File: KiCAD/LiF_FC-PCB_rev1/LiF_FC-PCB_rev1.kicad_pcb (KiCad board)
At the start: 4 copper layers, 70 x 90 mm, 203 parts, among them J13 ESP_DGB_CONN, J14 CAN Upstream, J15 ESP_DGB_CONN, J16 ESP_DGB_CONN, J19 Load Cell, J22 CAN Upstream, J28 CAN Downstream, J31 CAN, J37 SKP OUT, J40 Door Closed, J43 Servo A, J44 Servo B, J45 Conn_01x10_Socket, J46 Conn_01x16_Pin, J47 Conn_01x16_Pin, J7 V_{IN}, Q1 MMBT4401, Q2 MMBT4401, SW1 Flash, SW2 Reset, SW3 CAN Termination, U1 AZ1117-3.3, U10 MCP2542FD-E/SN, U11 BMA400, U12 PAM8302AAS, U13 NCA9555, U14 SN74HC14DR, U15 SN74HC14DR, U16 NCA9555, U2 AZ1117-3.3, U3 TPS2117DRLR, U4 TPS2117DRLR, U5 LMR14050, U6 ESP32-S3-WROOM-1, U7 CY7C65213-28PVXI, U8 MCP6N11-xxxE/SN, U9 NCV8114ASN165T1G

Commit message: routing in progress. backup save
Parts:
- SW3, TP22, TP23, TP24, TP28: moved to B.Cu
- moved R1 117.9 mm to (157.2, 58.5), turned to 180 degrees
- moved R5 112.6 mm to (152.2, 58.5), turned to 180 degrees
- moved SW3 84.6 mm to (130.5, 62.0), turned to 0 degrees
- moved C33 82.9 mm to (136.5, 65.5)
- moved U10 82.7 mm to (132.5, 67.0)
- moved C34 82.4 mm to (134.0, 72.5)
- moved D15 81.9 mm to (135.8, 56.0)
- moved R53 81.5 mm to (132.5, 61.2)
- moved TP24 72.3 mm to (139.8, 66.0)
- moved TP22 64.1 mm to (136.2, 61.0)
- moved TP23 60.7 mm to (126.2, 61.0)
- moved R46 47.8 mm to (57.8, 122.2)
- moved R48 47.8 mm to (57.8, 116.3)
- moved R47 16.4 mm to (121.2, 55.5)
- moved R63 12.3 mm to (152.5, 74.8)
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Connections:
- J47 pad 12: /Stackup Header/IO16 -> /Buttons/IO16
- J47 pad 13: /Stackup Header/IO17 -> /Buttons/IO17
- J47 pad 14: /Stackup Header/IO18 -> /Buttons/IO18
- J47 pad 15: /Stackup Header/IO19 -> /Buttons/IO19
- J47 pad 16: /Stackup Header/IO20 -> /Buttons/IO20
- J47 pad 17: /Stackup Header/IO21 -> /Buttons/IO21
- J47 pad 18: /Stackup Header/IO22 -> /Buttons/IO22
- J47 pad 19: /Stackup Header/IO23 -> /Buttons/IO23
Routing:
- net /CAN/CAN5V0_{OUT}: track 0.00 -> 54.0 mm
- net /Display/IO15: track 0.00 -> 28.9 mm
- net /Display/IO14: track 0.00 -> 26.1 mm
- net /Buttons/IN0: track 0.00 -> 25.0 mm
- net /Display/IO13: track 0.00 -> 23.3 mm
- net /Buttons/IN5: track 0.00 -> 21.9 mm
- net /Buttons/IN6: track 0.00 -> 21.7 mm
- net /Buttons/IN1: track 0.00 -> 21.3 mm
- net /Buttons/IN3: track 0.00 -> 20.5 mm
- net /Display/IO12: track 0.00 -> 20.5 mm
- net /Buttons/IN4: track 0.00 -> 20.3 mm
- net /Buttons/IO17: track 0.00 -> 18.0 mm
- net /Display/IO11: track 0.00 -> 17.7 mm
- net /Buttons/IO18: track 0.00 -> 17.3 mm
- net /Buttons/IO19: track 0.00 -> 16.9 mm
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
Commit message: routing backup
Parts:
- removed R39: 0, Resistor_SMD:R_0805_2012Metric
- TP1, TP2, TP25, TP26, TP29, TP3, TP4, TP5, TP6, TP9: moved to B.Cu
- moved R25 127.9 mm to (163.2, 121.8), turned to 180 degrees
- moved R66 121.4 mm to (163.5, 57.8), turned to -90 degrees
- moved R8 108.0 mm to (144.5, 89.5)
- moved R6 102.8 mm to (141.0, 75.0)
- moved TP1 95.7 mm to (161.2, 44.5)
- moved TP2 91.7 mm to (151.5, 66.0)
- moved R48 90.7 mm to (135.5, 69.5)
- moved R46 89.9 mm to (130.6, 69.5), turned to 180 degrees
- moved TP6 86.8 mm to (139.5, 93.8)
- moved TP9 84.2 mm to (143.5, 93.8)
- moved R35 84.1 mm to (120.2, 95.8), turned to 180 degrees
- moved TP5 83.7 mm to (147.5, 66.0)
- moved R7 82.8 mm to (114.5, 95.8)
- moved TP4 81.3 mm to (143.5, 66.0)
- moved R54 80.8 mm to (120.5, 85.5), turned to 180 degrees
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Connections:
- C25 pad 1: /Load Cell/LC_3V3 -> /A3V3
- C30 pad 1: /Load Cell/LC_3V3 -> /A3V3
- U8 pad 7: /Load Cell/LC_3V3 -> /A3V3
- U9 pad 1: /Load Cell/LC_3V3 -> /A3V3
- U9 pad 3: /Load Cell/LC_3V3 -> /A3V3
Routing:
- net GND: track 8.48 -> 61.5 mm, vias 3 -> 29
- net /Buttons/BTN3: track 0.00 -> 39.8 mm
- net /Buttons/BTN2: track 0.00 -> 39.5 mm
- net /Load Cell/E+: track 0.00 -> 38.7 mm, vias 0 -> 2
- net /Buttons/BTN1: track 0.00 -> 37.6 mm
- net /Buttons/BTN4: track 0.00 -> 35.6 mm
- net /Buttons/BTN0: track 0.00 -> 35.4 mm
- net /Buttons/BTN_3V3: track 0.00 -> 33.7 mm, vias 0 -> 4
- net /Buttons/BTN5: track 0.00 -> 32.5 mm
- net /Load Cell/V_{REF}: track 0.00 -> 26.5 mm
- net /MCU/ESP32_25: track 0.00 -> 24.6 mm, vias 0 -> 1
- net /A3V3: track 0.00 -> 22.5 mm, vias 0 -> 1
- net /Accelerometer/I2C.SCL: track 0.00 -> 22.4 mm
- net Net-(U8-V_{FG}): track 0.00 -> 21.2 mm
- net /Load Cell/A-: track 0.00 -> 19.7 mm
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- added copper zone on In2.Cu, net /MCU/ESP_3V3
- added copper zone on F.Cu, net /Power Regulation/5V Regulator/REG5V_in
- added copper zone on F.Cu, net /Power Regulation/5V Regulator/REG5V_out
- added copper zone on F.Cu, net /Power Regulation/5V Regulator/SW
- added copper zone on F.Cu, net /Power Regulation/A3V3_out
- added copper zone on F.Cu, net /Power Regulation/Power OR-ing/V_{IN1}
- added copper zone on F.Cu, net GND

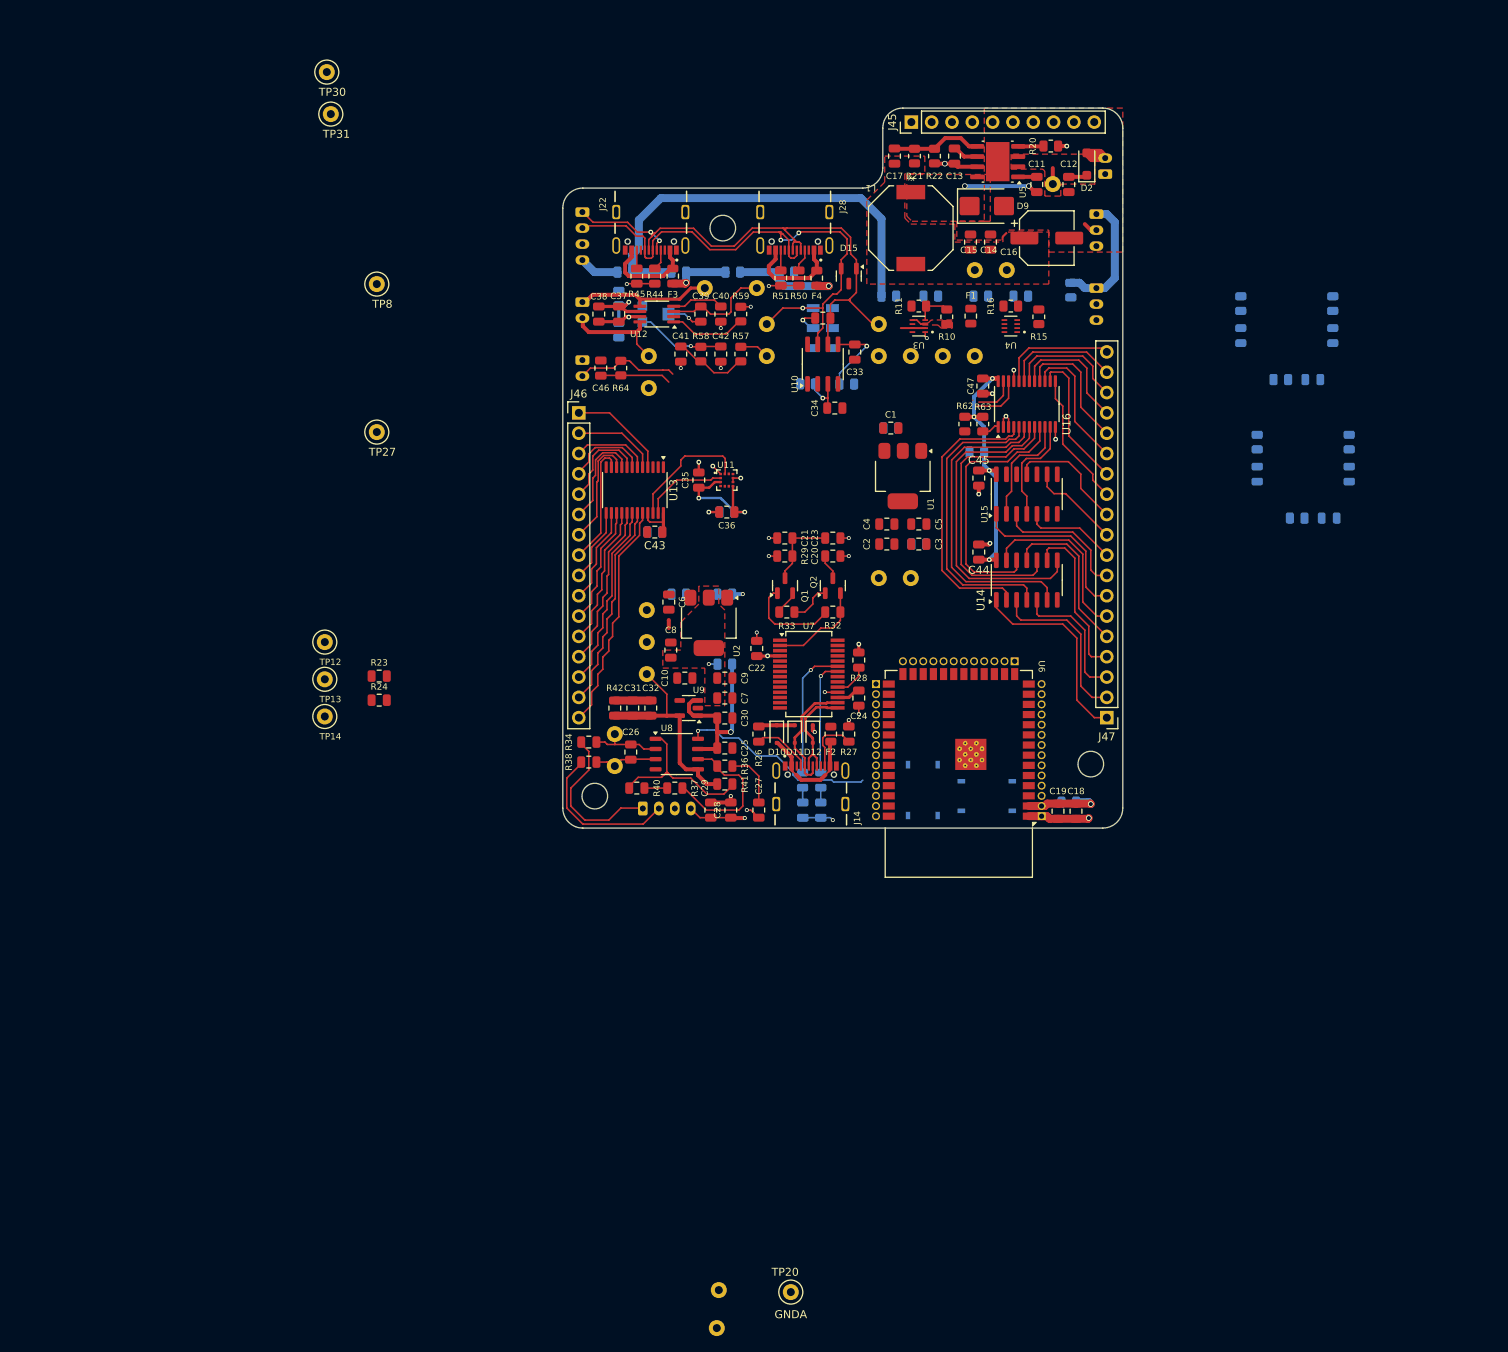
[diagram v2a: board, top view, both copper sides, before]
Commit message: finished service PCB routing and silkscreen, finished IO PCB layout, routing, and silkscreen. Exported production files, submitted PCB for manufacturing by JLCPCB
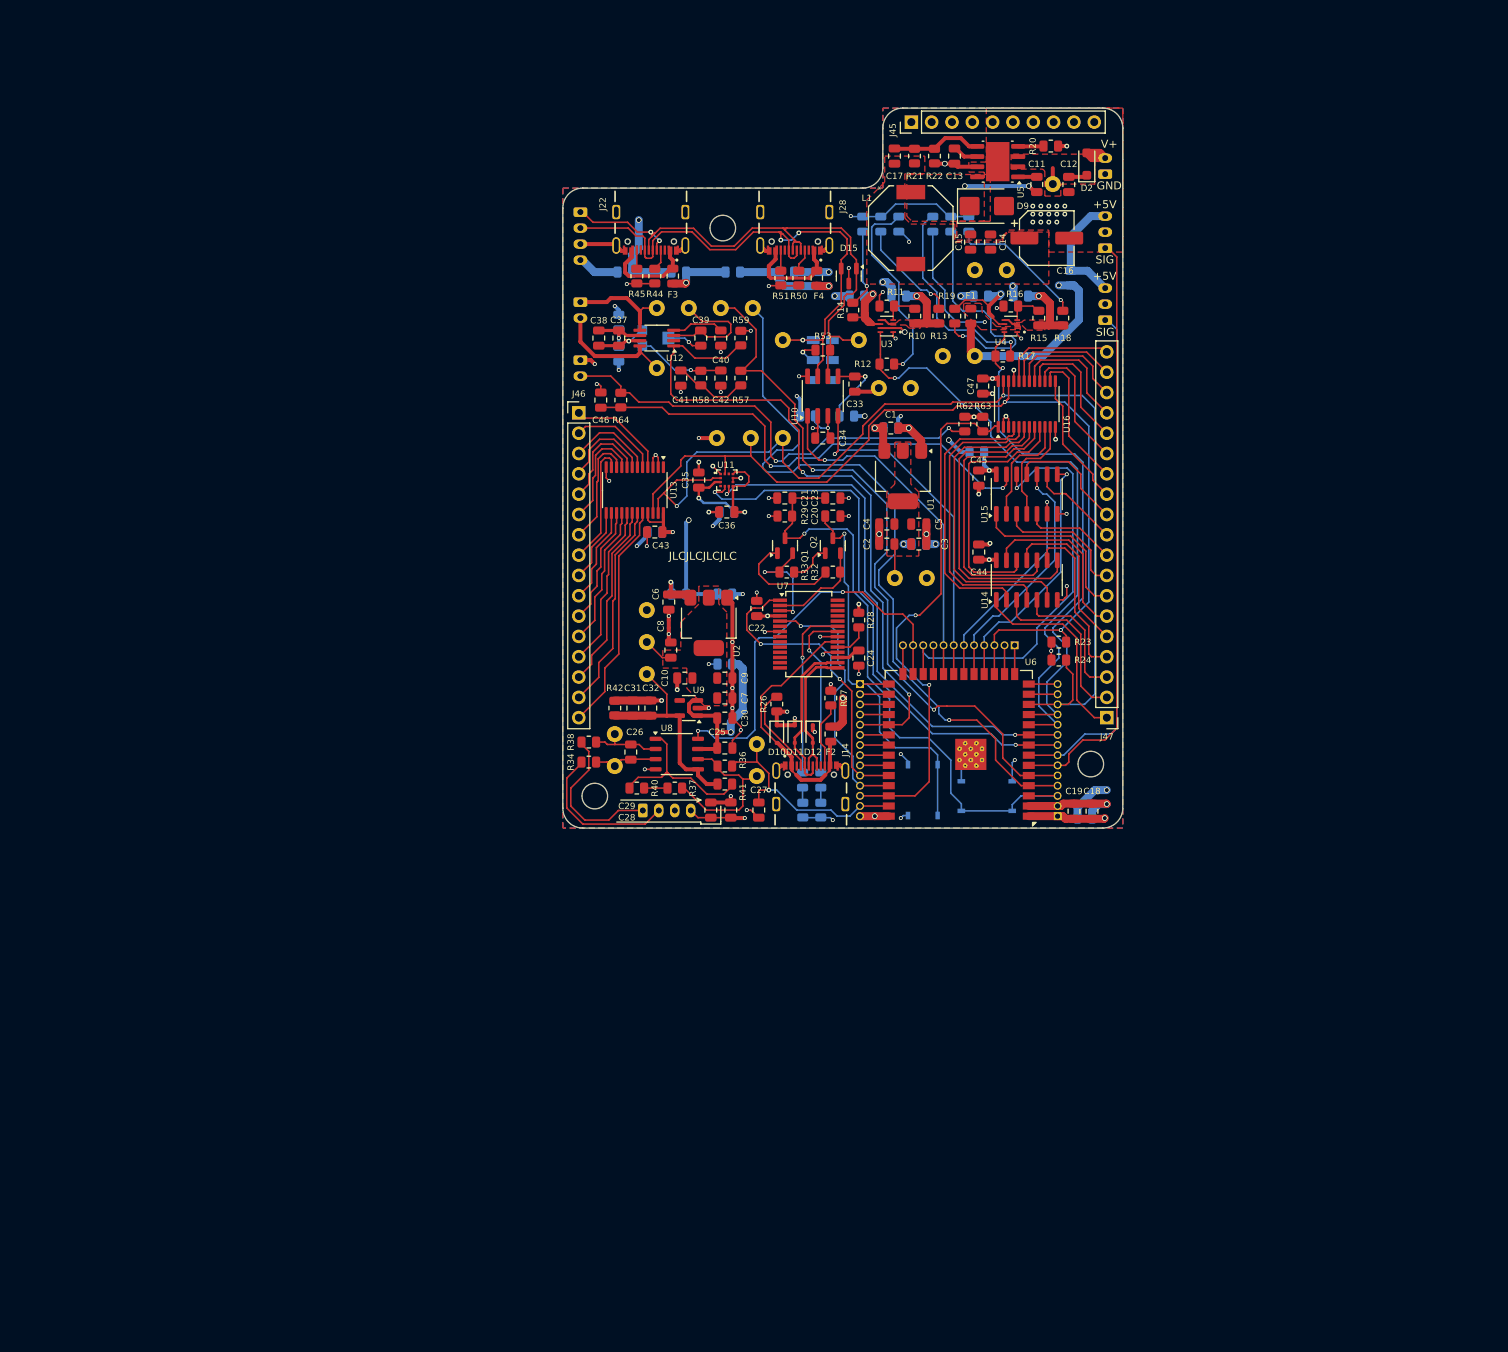
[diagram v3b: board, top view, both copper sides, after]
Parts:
- removed TP20: GNDA, TestPoint:TestPoint_Loop_D1.80mm_Drill1.0mm_Beaded
- removed TP3, TP8: GND, TestPoint:TestPoint_Loop_D1.80mm_Drill1.0mm_Beaded
- removed TP30: SRV_{A}, TestPoint:TestPoint_Loop_D1.80mm_Drill1.0mm_Beaded
- removed TP31: SRV_{B}, TestPoint:TestPoint_Loop_D1.80mm_Drill1.0mm_Beaded
- R12, R13, R14, R17, R18, R19: moved to F.Cu
- R23, R24, R26, R27, R28, R29, R30, R31, R32, R33, R34, R36, R37, R38, R40, R41, R42, R44, R45, R50, R51, R53: footprint Capacitor_SMD:C_0805_2012Metric -> Resistor_SMD:R_0805_2012Metric
- SW3: footprint LiF_PCB_Footprints:SW_JS202011JCQN -> Button_Switch_SMD:SW_DPDT_CK_JS202011JCQN
- TP12, TP13, TP14, TP27: moved to B.Cu
- moved R24 85.1 mm to (162.0, 104.0), turned to 180 degrees
- moved R23 85.1 mm to (162.0, 101.8), turned to 180 degrees
- moved TP17 69.2 mm to (124.2, 118.5)
- moved TP18 68.4 mm to (124.2, 114.5)
- moved D5 68.4 mm to (137.5, 49.5)
- moved TP14 67.0 mm to (127.5, 76.2)
- moved D3 65.2 mm to (142.0, 49.5), turned to -90 degrees
- moved R14 64.2 mm to (136.2, 60.2), turned to -90 degrees
- moved TP13 61.2 mm to (123.5, 76.2)
- moved D4 56.5 mm to (139.8, 49.5)
- moved TP12 55.2 mm to (119.2, 76.2)
- moved R12 54.8 mm to (140.5, 67.0)
- moved D6 51.3 mm to (146.2, 49.5), turned to -90 degrees
- moved D8 49.7 mm to (148.5, 49.5)
- moved TP27 49.5 mm to (123.8, 60.0)
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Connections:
- D2 pad 2: /Power Regulation/V_{supply} -> /Stackup Header/V_{supply}
- D4 pad 1: Net-(D4-K) -> GND
- D4 pad 2: /Power Regulation/Power OR-ing/V_{IN1} -> Net-(D4-A)
- D5 pad 1: Net-(D5-K) -> GND
- D5 pad 2: /Power Regulation/Power OR-ing/V_{IN2} -> Net-(D5-A)
- D7 pad 1: Net-(D7-K) -> GND
- D7 pad 2: /Power Regulation/Power OR-ing1/V_{IN1} -> Net-(D7-A)
- D8 pad 1: Net-(D8-K) -> GND
- D8 pad 2: /Power Regulation/Power OR-ing1/V_{IN2} -> Net-(D8-A)
- J13 pad 10: /MCU/V_{ST}.SYS -> /MCU/V_{ST}.AUX
- J13 pad 11: /MCU/V_{ST}.AUX -> /MCU/V_{ST}.SYS
- J19 pad 3: /Load Cell/E- -> GNDA
- J43 pad 1: /Servos/SRV_5V0 -> /MCU/SRV.A
- J43 pad 3: /MCU/SRV.A -> /Servos/SRV_5V0
- J44 pad 1: /Servos/SRV_5V0 -> /MCU/SRV.B
- J44 pad 3: /MCU/SRV.B -> /Servos/SRV_5V0
- J45 pad 1: /SYS5V0 -> GND
- J45 pad 10: unconnected-(J45-Pin_10-Pad10) -> GND
- J45 pad 2: unconnected-(J45-Pin_2-Pad2) -> GND
- J45 pad 3: unconnected-(J45-Pin_3-Pad3) -> GND
- J45 pad 4: unconnected-(J45-Pin_4-Pad4) -> /R3V3
- J45 pad 5: unconnected-(J45-Pin_5-Pad5) -> /R3V3
- J45 pad 6: unconnected-(J45-Pin_6-Pad6) -> /SYS5V0
- J45 pad 7: unconnected-(J45-Pin_7-Pad7) -> /SYS5V0
- J45 pad 8: unconnected-(J45-Pin_8-Pad8) -> /Stackup Header/V_{supply}
- J45 pad 9: unconnected-(J45-Pin_9-Pad9) -> /Stackup Header/V_{supply}
- J7 pad 2: /Power Regulation/V_{supply} -> /Stackup Header/V_{supply}
- R13 pad 1: Net-(D4-K) -> Net-(D4-A)
- R13 pad 2: GND -> /Power Regulation/Power OR-ing/V_{IN1}
- R14 pad 1: Net-(D5-K) -> Net-(D5-A)
- R14 pad 2: GND -> /Power Regulation/Power OR-ing/V_{IN2}
- R18 pad 1: Net-(D7-K) -> Net-(D7-A)
- R18 pad 2: GND -> /Power Regulation/Power OR-ing1/V_{IN1}
- R19 pad 1: Net-(D8-K) -> Net-(D8-A)
- R19 pad 2: GND -> /Power Regulation/Power OR-ing1/V_{IN2}
- R53 pad 2: Net-(SW3B-C) -> Net-(SW3B-B)
- SW3 pad 5: /CAN/CAN+ -> Net-(SW3B-B)
- SW3 pad 6: Net-(SW3B-C) -> /CAN/CAN+
- U6 pad 10: /MCU/V_{ST}.SYS -> /MCU/V_{ST}.AUX
- U6 pad 11: /MCU/V_{ST}.AUX -> /MCU/V_{ST}.SYS
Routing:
- net /SYS5V0: track 0.00 -> 144.3 mm, vias 0 -> 5
- net /Accelerometer/I2C.SDA: track 15.9 -> 134.3 mm, vias 0 -> 2
- net /Audio/PDM.CLK: track 0.00 -> 95.1 mm, vias 0 -> 1
- net /Accelerometer/I2C.SCL: track 22.4 -> 117.2 mm, vias 0 -> 2
- net /MCU/V_{PROG USB}: track 0.00 -> 91.7 mm, vias 0 -> 2
- net GND: track 61.5 -> 151.5 mm, vias 29 -> 70
- net /Audio/PDM.DATA: track 3.73 -> 90.7 mm, vias 0 -> 2
- net /MCU/V_{ST}.AUX: track 0.00 -> 76.6 mm, vias 0 -> 1
- net /Audio/AMP_{EN}: track 9.68 -> 86.1 mm, vias 0 -> 2
- net /MCU/SRV.A: track 0.00 -> 74.3 mm
- net /Accelerometer/ACC_INT1: track 0.00 -> 70.4 mm, vias 0 -> 2
- net /MCU/CHIP_PU: track 9.49 -> 77.8 mm, vias 0 -> 1
- net /Accelerometer/ACC_INT2: track 0.00 -> 67.6 mm, vias 0 -> 2
- net /MCU/V_{ST}.SYS: track 0.00 -> 64.7 mm, vias 0 -> 1
- net /Buttons/~{BTN_IRQ}: track 2.25 -> 66.9 mm, vias 0 -> 2
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- added copper zone on F.Cu, net /Power Regulation/Power OR-ing1/V_{IN1}
- added copper zone on F.Cu, net /Power Regulation/Power OR-ing1/V_{out}
- added copper zone on F.Cu, net /Power Regulation/R3V3_out
- added copper zone on In2.Cu, net /R3V3
- added copper zone on B.Cu, net GND
- added copper zone on In1.Cu, net GND
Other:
- board text added: "+5V"
- board text added: "0"
- board text added: "1"
- board text added: "1.25W"
- board text added: "10"
- board text added: "11"
- board text added: "12"
- board text added: "120Ω"
- board text added: "13"
- board text added: "14"
- board text added: "15"
- board text added: "16"
- board text added: "17"
- board text added: "18"
- board text added: "2"
- board text added: "2.5W"
- board text added: "2026-07 MR NK RY"
- board text added: "21"
- board text added: "3"
- board text added: "35"
- board text added: "36"
- board text added: "37"
- board text added: "38"
- board text added: "39"
- board text added: "3V3"
- board text added: "4"
- board text added: "40"
- board text added: "41"
- board text added: "42"
- board text added: "45"
- board text added: "46"
- board text added: "47"
- board text added: "48"
- board text added: "5"
- board text added: "6"
- board text added: "7"
- board text added: "7SEG_{EN}"
- board text added: "8"
- board text added: "9"
- board text added: "A3V3_{EN}"
- board text added: "ACC_{EN}"
- board text added: "AUX"
- board text added: "Audio"
- board text added: "BTN_{EN}"
- board text added: "BUS"
- board text added: "BUS PWR OPT"
- board text added: "BUS PWR STATUS"
- board text added: "CAN"
- board text added: "CAN_{3V3}"
- board text added: "CLK"
- board text added: "D+"
- board text added: "D-"
- board text added: "DATA"
- board text added: "EN"
- board text added: "ESP32-S3"
- board text added: "ESP_{EN}"
- board text added: "Floor Controller rev1"
- board text added: "GND"
- board text added: "IN"
- board text added: "IN0"
- board text added: "IN1"
- board text added: "IN10"
- board text added: "IN16"
- board text added: "IN17"
- board text added: "IN18"
- board text added: "IN19"
- board text added: "IN2"
- board text added: "IN20"
- board text added: "IN21"
- board text added: "IN22"
- board text added: "IN23"
- board text added: "IN3"
- board text added: "IN4"
- board text added: "IN5"
- board text added: "IN6"
- board text added: "IN7"
- board text added: "IN8"
- board text added: "IN9"
- board text added: "IO0"
- board text added: "IO1"
- board text added: "IO10"
- board text added: "IO11"
- board text added: "IO12"
- board text added: "IO13"
- board text added: "IO14"
- board text added: "IO15"
- board text added: "IO2"
- board text added: "IO3"
- board text added: "IO4"
- board text added: "IO5"
- board text added: "IO6"
- board text added: "IO7"
- board text added: "IO8"
- board text added: "IO9"
- board text added: "I^{2}C"
- board text added: "JLCJLCJLCJLC"
- board text added: "LC3V_{EN}"
- board text added: "LC5V_{EN}"
- board text added: "ON"
- board text added: "OUT"
- board text added: "PATH"
- board text added: "PDM"
- board text added: "PRG"
- board text added: "PWR"
- board text added: "Project Lithium Firefly"
- board text added: "R3VE_{EN}"
- board text added: "R3VE_{OUT}"
- board text added: "REF"
- board text added: "RX"
- board text added: "SCL"
- board text added: "SDA"
- board text added: "SETTING"
- board text added: "SIG"
- board text added: "SPK"
- board text added: "SYS PWR OPT"
- board text added: "SYS PWR STATUS"
- board text added: "TX"
- board text added: "UART PROG"
- board text added: "V+"
- board text added: "VOL"
- board text added: "_{a}AUX"
- board text added: "_{a}BUS"
- board text added: "_{b}CAN"
- board text added: "_{b}PRG"
- board text added: "b/~{a}"
- board text removed: "1 2"
- board text removed: "3 4"
- board text removed: "5 6"
- board text removed: "door call"
